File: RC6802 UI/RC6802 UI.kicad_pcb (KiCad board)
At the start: 2 copper layers, 99.1 x 86.4 mm, 80 parts, among them J1 TAPE, J2 RC6802_UI_Port, J3 EXT_KEYPAD, M1 Mounting, M2 Mounting, M3 Mounting, M4 Mounting, Q1 2N3906, Q2 2N3906, Q3 2N3904, Q4 2N3904, Q5 2N3904, SW1 RESET, SW10 D, SW11 2, SW12 6, SW13 A, SW14 E, SW15 3, SW16 7, SW17 B, SW18 F, SW19 TAPE, SW2 SW_SST, SW20 STEP, SW21 HW_SST, SW3 Ø, SW4 4, SW5 8, SW6 C, SW7 1, SW8 5, SW9 9, U1 74LS374, U2 74LS00, U3 74LS73

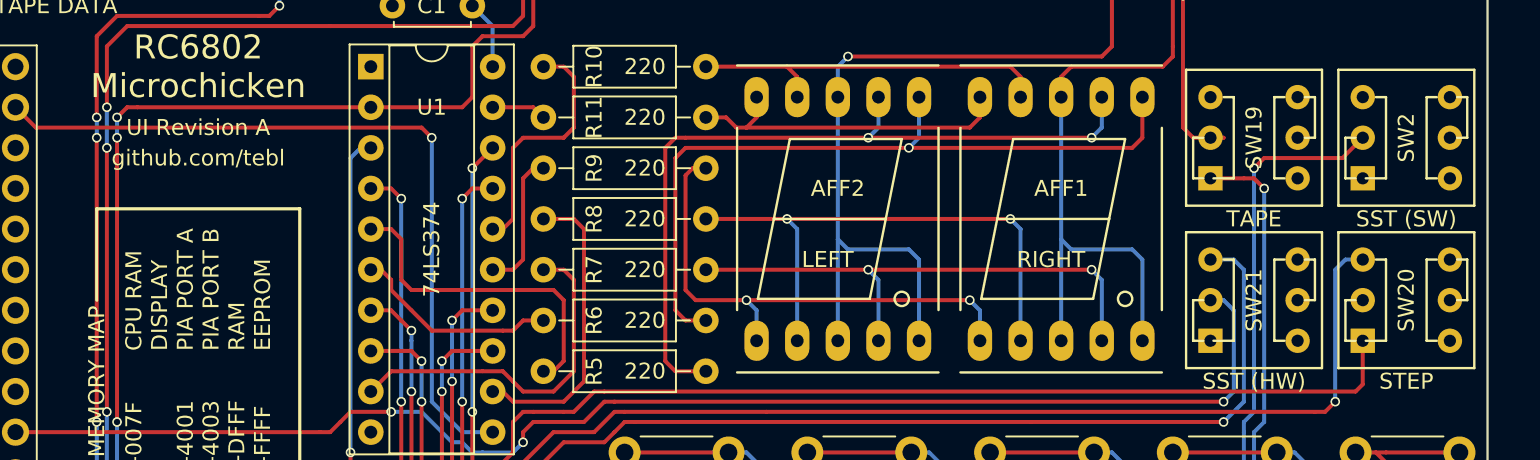
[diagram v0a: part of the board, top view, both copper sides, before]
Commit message: Updated UI to change footprints
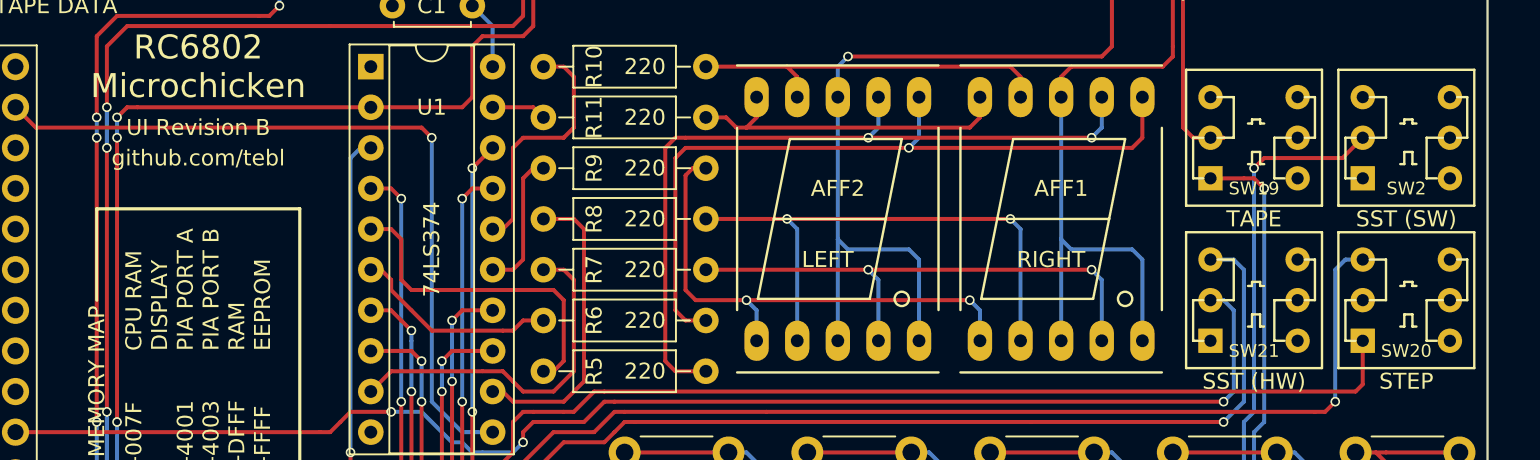
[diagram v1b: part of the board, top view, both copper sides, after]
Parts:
- SW19, SW2, SW20, SW21: footprint DPDT_Switch:dpdt_switch -> DPDT_Switch:dpdt_switch_black
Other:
- board text added: "C.A."
- board text added: "UI Revision B"
- board text removed: "UI Revision A"

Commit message: Revision B build
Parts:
- SW2: value SW_SST -> ~IRQ
- SW21: value HW_SST -> SST
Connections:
- SW19 pad 1: /PB7 -> (no net)
- SW19 pad 3: (no net) -> /PB7
- SW2 pad 1: GND -> (no net)
- SW2 pad 3: (no net) -> GND
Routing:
- net /PB7: track 141.0 -> 146.1 mm
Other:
- board text added: "SST"
- board text added: "~IRQ"
- board text removed: "SST (HW)"
- board text removed: "SST (SW)"
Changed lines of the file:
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@@
     (links 217)
     (no_connects 0)
-    (area 100.254999 57.709999 199.465001 144.220001)
+    (area 93.345 43.815 205.730001 161.290001)
     (thickness 1.6)
     (drawings 101)
-    (tracks 1114)
+    (tracks 1115)
     (zones 0)
     (modules 80)
@@
       (effects (font (size 0.8 0.8) (thickness 0.1)))
     )
-    (fp_text value SW_SST (at 0 -3.81) (layer F.Fab)
+    (fp_text value ~IRQ (at 0 -3.81) (layer F.Fab)
       (effects (font (size 0.8 0.8) (thickness 0.1)))
     )
@@
     (fp_line (start -4.25 -4.25) (end -4.25 4.25) (layer F.SilkS) (width 0.15))
     (fp_line (start -4.25 4.25) (end 4.25 4.25) (layer F.SilkS) (width 0.15))
-    (pad 3 thru_hole circle (at -2.725 -2.54) (size 1.524 1.524) (drill 0.762) (layers *.Cu *.Mask))
+    (pad 3 thru_hole circle (at -2.725 -2.54) (size 1.524 1.524) (drill 0.762) (layers *.Cu *.Mask)
+      (net 1 GND))
     (pad 2 thru_hole circle (at -2.725 0) (size 1.524 1.524) (drill 0.762) (layers *.Cu *.Mask)
       (net 25 ~SST))
-    (pad 1 thru_hole rect (at -2.725 2.54) (size 1.524 1.524) (drill 0.762) (layers *.Cu *.Mask)
-      (net 1 GND))
+    (pad 1 thru_hole rect (at -2.725 2.54) (size 1.524 1.524) (drill 0.762) (layers *.Cu *.Mask))
     (pad 4 thru_hole circle (at 2.725 2.54) (size 1.524 1.524) (drill 0.762) (layers *.Cu *.Mask))
     (pad 5 thru_hole circle (at 2.725 0) (size 1.524 1.524) (drill 0.762) (layers *.Cu *.Mask))
@@
     (fp_line (start -4.25 -4.25) (end -4.25 4.25) (layer F.SilkS) (width 0.15))
     (fp_line (start -4.25 4.25) (end 4.25 4.25) (layer F.SilkS) (width 0.15))
-    (pad 3 thru_hole circle (at -2.725 -2.54) (size 1.524 1.524) (drill 0.762) (layers *.Cu *.Mask))
+    (pad 3 thru_hole circle (at -2.725 -2.54) (size 1.524 1.524) (drill 0.762) (layers *.Cu *.Mask)
+      (net 29 /PB7))
     (pad 2 thru_hole circle (at -2.725 0) (size 1.524 1.524) (drill 0.762) (layers *.Cu *.Mask)
       (net 49 "Net-(Q3-Pad3)"))
-    (pad 1 thru_hole rect (at -2.725 2.54) (size 1.524 1.524) (drill 0.762) (layers *.Cu *.Mask)
-      (net 29 /PB7))
+    (pad 1 thru_hole rect (at -2.725 2.54) (size 1.524 1.524) (drill 0.762) (layers *.Cu *.Mask))
     (pad 4 thru_hole circle (at 2.725 2.54) (size 1.524 1.524) (drill 0.762) (layers *.Cu *.Mask))
     (pad 5 thru_hole circle (at 2.725 0) (size 1.524 1.524) (drill 0.762) (layers *.Cu *.Mask))
@@
       (effects (font (size 0.8 0.8) (thickness 0.1)))
     )
-    (fp_text value HW_SST (at 0 -3.81) (layer F.Fab)
+    (fp_text value SST (at 0 -3.81) (layer F.Fab)
       (effects (font (size 0.8 0.8) (thickness 0.1)))
     )
@@
     (effects (font (size 0.8 0.8) (thickness 0.1)) (justify mirror))
   )
-  (gr_text "SST (SW)" (at 194.31 93.345) (layer F.SilkS)
+  (gr_text ~IRQ (at 194.31 93.345) (layer F.SilkS)
     (effects (font (size 1 1) (thickness 0.15)))
   )
-  (gr_text "SST (HW)" (at 184.785 103.505) (layer F.SilkS)
+  (gr_text SST (at 184.785 103.505) (layer F.SilkS)
     (effects (font (size 1 1) (thickness 0.15)))
   )
@@
   (segment (start 120.015 114.3) (end 133.35 114.3) (width 0.25) (layer F.Cu) (net 28))
   (segment (start 135.255 99.06) (end 137.16 99.06) (width 0.25) (layer F.Cu) (net 28))
+  (segment (start 182.06 85.725) (end 184.785 85.725) (width 0.25) (layer F.Cu) (net 29))
+  (segment (start 185.42 88.265) (end 185.42 91.44) (width 0.25) (layer B.Cu) (net 29))
+  (via (at 185.42 88.265) (size 0.6) (drill 0.4) (layers F.Cu B.Cu) (net 29))
+  (segment (start 185.42 86.36) (end 185.42 88.265) (width 0.25) (layer F.Cu) (net 29))
+  (segment (start 184.785 85.725) (end 185.42 86.36) (width 0.25) (layer F.Cu) (net 29))
   (segment (start 184.785 106.68) (end 185.42 106.045) (width 0.25) (layer B.Cu) (net 29))
-  (segment (start 184.785 90.805) (end 184.15 90.805) (width 0.25) (layer F.Cu) (net 29))
-  (segment (start 185.42 91.44) (end 184.785 90.805) (width 0.25) (layer F.Cu) (net 29))
-  (via (at 185.42 91.44) (size 0.6) (drill 0.4) (layers F.Cu B.Cu) (net 29))
   (segment (start 185.42 106.045) (end 185.42 91.44) (width 0.25) (layer B.Cu) (net 29))
   (segment (start 184.15 124.46) (end 184.785 123.825) (width 0.25) (layer F.Cu) (net 29))
@@
   (segment (start 140.335 134.62) (end 142.24 132.715) (width 0.25) (layer F.Cu) (net 29))
   (segment (start 150.495 124.46) (end 184.15 124.46) (width 0.25) (layer F.Cu) (net 29))
-  (segment (start 184.15 90.805) (end 182.06 90.805) (width 0.25) (layer F.Cu) (net 29))
   (segment (start 113.03 113.665) (end 112.395 113.665) (width 0.25) (layer F.Cu) (net 30))
   (segment (start 110.49 115.57) (end 110.49 116.205) (width 0.25) (layer F.Cu) (net 30))

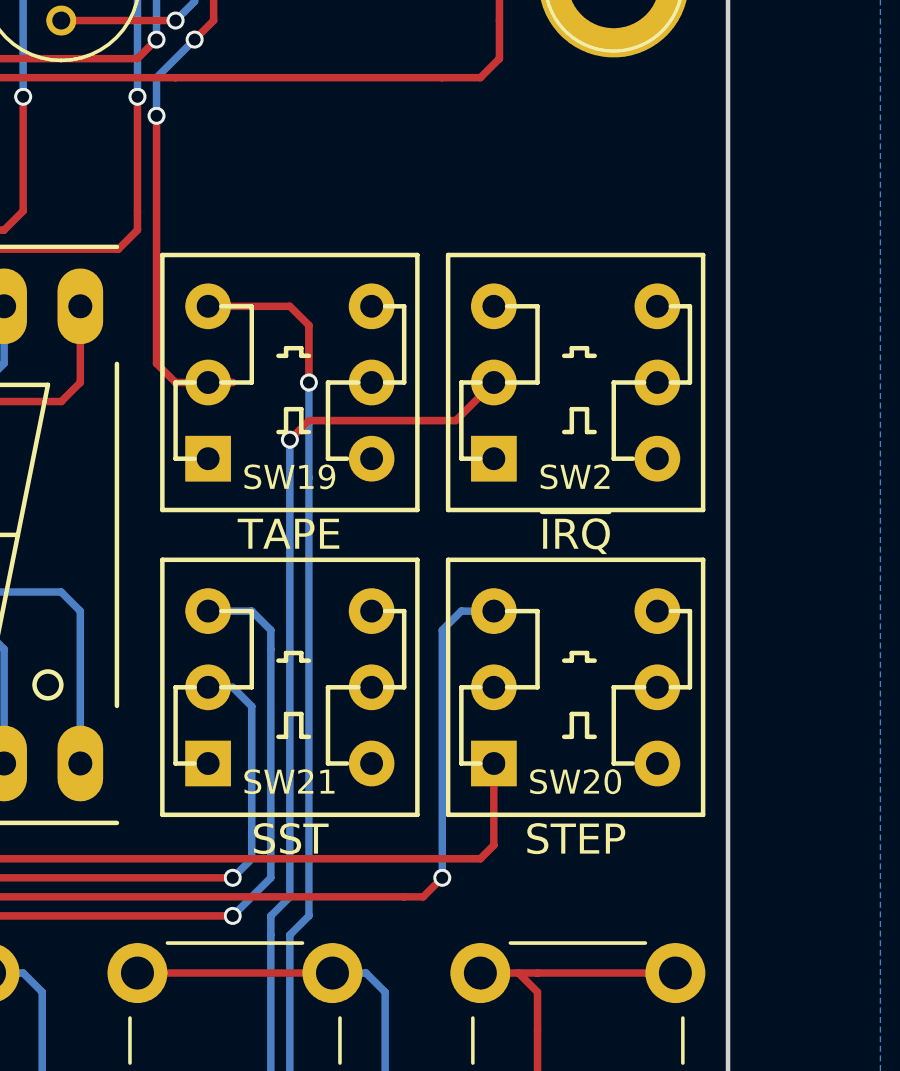
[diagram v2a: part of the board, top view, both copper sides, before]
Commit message: UI silkscreen improved
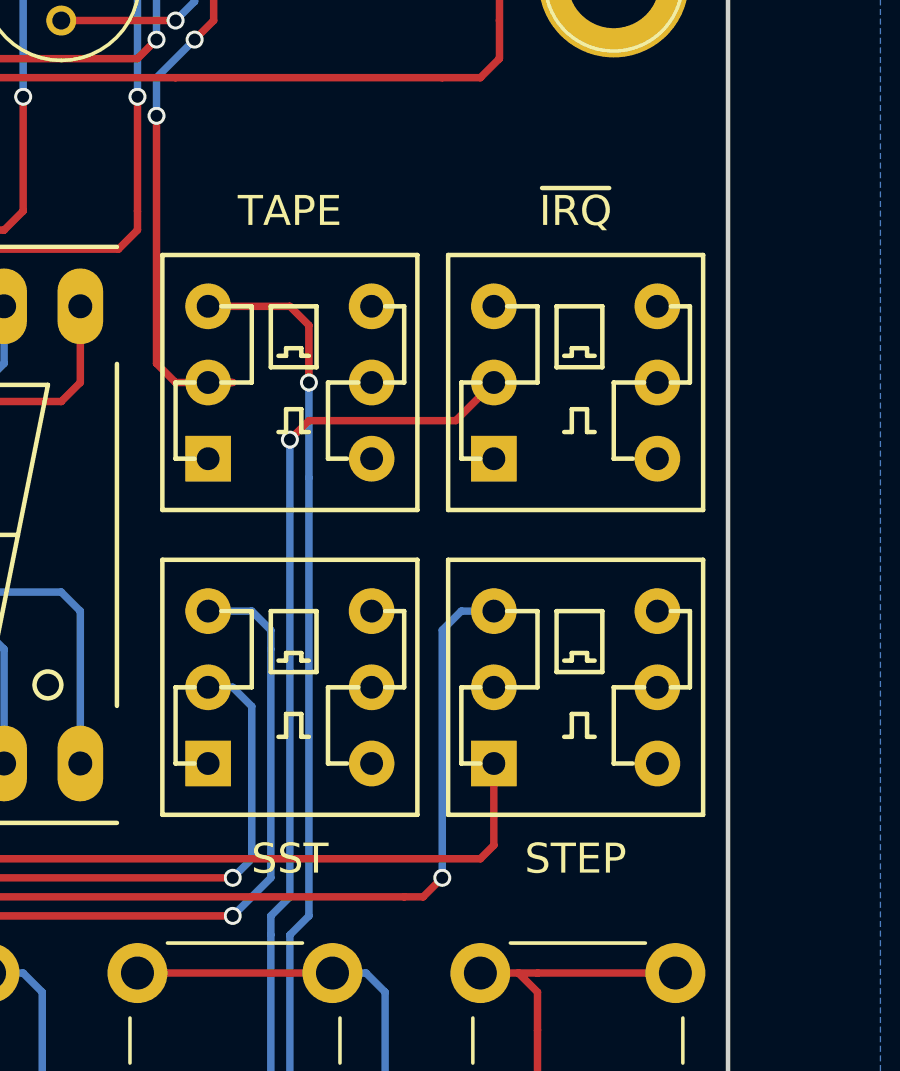
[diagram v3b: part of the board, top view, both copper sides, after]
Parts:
- SW19, SW2, SW20, SW21: footprint DPDT_Switch:dpdt_switch_black -> DPDT_Switch:dpdt_switch
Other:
- board text removed: "SST"
- board text removed: "~IRQ"
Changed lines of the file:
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@@
     (links 217)
     (no_connects 0)
-    (area 93.345 43.815 205.730001 161.290001)
+    (area 100.254999 57.709999 199.465001 144.220001)
     (thickness 1.6)
-    (drawings 101)
+    (drawings 99)
     (tracks 1115)
     (zones 0)
@@
     )
   )
-  (module DPDT_Switch:dpdt_switch_black (layer F.Cu)
+  (module DPDT_Switch:dpdt_switch (layer F.Cu)
     (at 194.31 88.265)
-    (fp_text reference SW2 (at 0 3.175) (layer F.SilkS)
-      (effects (font (size 0.8 0.8) (thickness 0.1)))
+    (fp_text reference SW2 (at 0 3.175) (layer F.Fab)
+      (effects (font (size 1 1) (thickness 0.15)))
     )
-    (fp_text value ~IRQ (at 0 -3.81) (layer F.Fab)
-      (effects (font (size 0.8 0.8) (thickness 0.1)))
+    (fp_text value ~IRQ (at 0 -5.715) (layer F.SilkS)
+      (effects (font (size 1 1) (thickness 0.15)))
     )
+    (fp_line (start -0.635 -0.508) (end -0.635 -2.54) (layer F.SilkS) (width 0.15))
+    (fp_line (start 0.889 -2.54) (end 0.889 -0.508) (layer F.SilkS) (width 0.15))
+    (fp_line (start -0.635 -0.508) (end 0.889 -0.508) (layer F.SilkS) (width 0.15))
+    (fp_line (start 0.889 -2.54) (end -0.635 -2.54) (layer F.SilkS) (width 0.15))
     (fp_line (start -0.381 -0.889) (end -0.127 -0.889) (layer F.SilkS) (width 0.15))
     (fp_line (start -0.127 -0.889) (end -0.127 -1.143) (layer F.SilkS) (width 0.15))
@@
     (pad 6 thru_hole circle (at 2.725 -2.54) (size 1.524 1.524) (drill 0.762) (layers *.Cu *.Mask))
   )
-  (module DPDT_Switch:dpdt_switch_black (layer F.Cu)
+  (module DPDT_Switch:dpdt_switch (layer F.Cu)
     (at 184.785 88.265)
-    (fp_text reference SW19 (at 0 3.175) (layer F.SilkS)
-      (effects (font (size 0.8 0.8) (thickness 0.1)))
+    (fp_text reference SW19 (at 0 3.175) (layer F.Fab)
+      (effects (font (size 1 1) (thickness 0.15)))
     )
-    (fp_text value TAPE (at 0 5.08) (layer F.SilkS)
+    (fp_text value TAPE (at 0 -5.715) (layer F.SilkS)
       (effects (font (size 1 1) (thickness 0.15)))
     )
+    (fp_line (start -0.635 -0.508) (end -0.635 -2.54) (layer F.SilkS) (width 0.15))
+    (fp_line (start 0.889 -2.54) (end 0.889 -0.508) (layer F.SilkS) (width 0.15))
+    (fp_line (start -0.635 -0.508) (end 0.889 -0.508) (layer F.SilkS) (width 0.15))
+    (fp_line (start 0.889 -2.54) (end -0.635 -2.54) (layer F.SilkS) (width 0.15))
     (fp_line (start -0.381 -0.889) (end -0.127 -0.889) (layer F.SilkS) (width 0.15))
     (fp_line (start -0.127 -0.889) (end -0.127 -1.143) (layer F.SilkS) (width 0.15))
@@
     (pad 6 thru_hole circle (at 2.725 -2.54) (size 1.524 1.524) (drill 0.762) (layers *.Cu *.Mask))
   )
-  (module DPDT_Switch:dpdt_switch_black (layer F.Cu)
+  (module DPDT_Switch:dpdt_switch (layer F.Cu)
     (at 194.31 98.425)
-    (fp_text reference SW20 (at 0 3.175) (layer F.SilkS)
-      (effects (font (size 0.8 0.8) (thickness 0.1)))
+    (fp_text reference SW20 (at 0 3.175) (layer F.Fab)
+      (effects (font (size 1 1) (thickness 0.15)))
     )
-    (fp_text value STEP (at 0 5.08) (layer F.SilkS)
+    (fp_text value STEP (at 0 5.715) (layer F.SilkS)
       (effects (font (size 1 1) (thickness 0.15)))
     )
+    (fp_line (start -0.635 -0.508) (end -0.635 -2.54) (layer F.SilkS) (width 0.15))
+    (fp_line (start 0.889 -2.54) (end 0.889 -0.508) (layer F.SilkS) (width 0.15))
+    (fp_line (start -0.635 -0.508) (end 0.889 -0.508) (layer F.SilkS) (width 0.15))
+    (fp_line (start 0.889 -2.54) (end -0.635 -2.54) (layer F.SilkS) (width 0.15))
     (fp_line (start -0.381 -0.889) (end -0.127 -0.889) (layer F.SilkS) (width 0.15))
     (fp_line (start -0.127 -0.889) (end -0.127 -1.143) (layer F.SilkS) (width 0.15))
@@
     (pad 6 thru_hole circle (at 2.725 -2.54) (size 1.524 1.524) (drill 0.762) (layers *.Cu *.Mask))
   )
-  (module DPDT_Switch:dpdt_switch_black (layer F.Cu)
+  (module DPDT_Switch:dpdt_switch (layer F.Cu)
     (at 184.785 98.425)
-    (fp_text reference SW21 (at 0 3.175) (layer F.SilkS)
-      (effects (font (size 0.8 0.8) (thickness 0.1)))
+    (fp_text reference SW21 (at 0 3.175) (layer F.Fab)
+      (effects (font (size 1 1) (thickness 0.15)))
     )
-    (fp_text value SST (at 0 -3.81) (layer F.Fab)
-      (effects (font (size 0.8 0.8) (thickness 0.1)))
+    (fp_text value SST (at 0 5.715) (layer F.SilkS)
+      (effects (font (size 1 1) (thickness 0.15)))
     )
+    (fp_line (start -0.635 -0.508) (end -0.635 -2.54) (layer F.SilkS) (width 0.15))
+    (fp_line (start 0.889 -2.54) (end 0.889 -0.508) (layer F.SilkS) (width 0.15))
+    (fp_line (start -0.635 -0.508) (end 0.889 -0.508) (layer F.SilkS) (width 0.15))
+    (fp_line (start 0.889 -2.54) (end -0.635 -2.54) (layer F.SilkS) (width 0.15))
     (fp_line (start -0.381 -0.889) (end -0.127 -0.889) (layer F.SilkS) (width 0.15))
     (fp_line (start -0.127 -0.889) (end -0.127 -1.143) (layer F.SilkS) (width 0.15))
@@
     (effects (font (size 0.8 0.8) (thickness 0.1)) (justify mirror))
   )
-  (gr_text ~IRQ (at 194.31 93.345) (layer F.SilkS)
-    (effects (font (size 1 1) (thickness 0.15)))
-  )
-  (gr_text SST (at 184.785 103.505) (layer F.SilkS)
-    (effects (font (size 1 1) (thickness 0.15)))
-  )
   (gr_line (start 161.29 105.41) (end 142.875 105.41) (angle 90) (layer B.SilkS) (width 0.2))
